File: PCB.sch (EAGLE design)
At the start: 38 parts, among them IC1 MAX13448E, IC2 MAX13487E, IC3 LP2981A-50_DBV_5, IC4 TXB0101, IC5 TXB0101, IC6 SN74LVC2G04_DBV_6, IC7 MAX232E, IC8 SN74LVC1G11_DBV_6

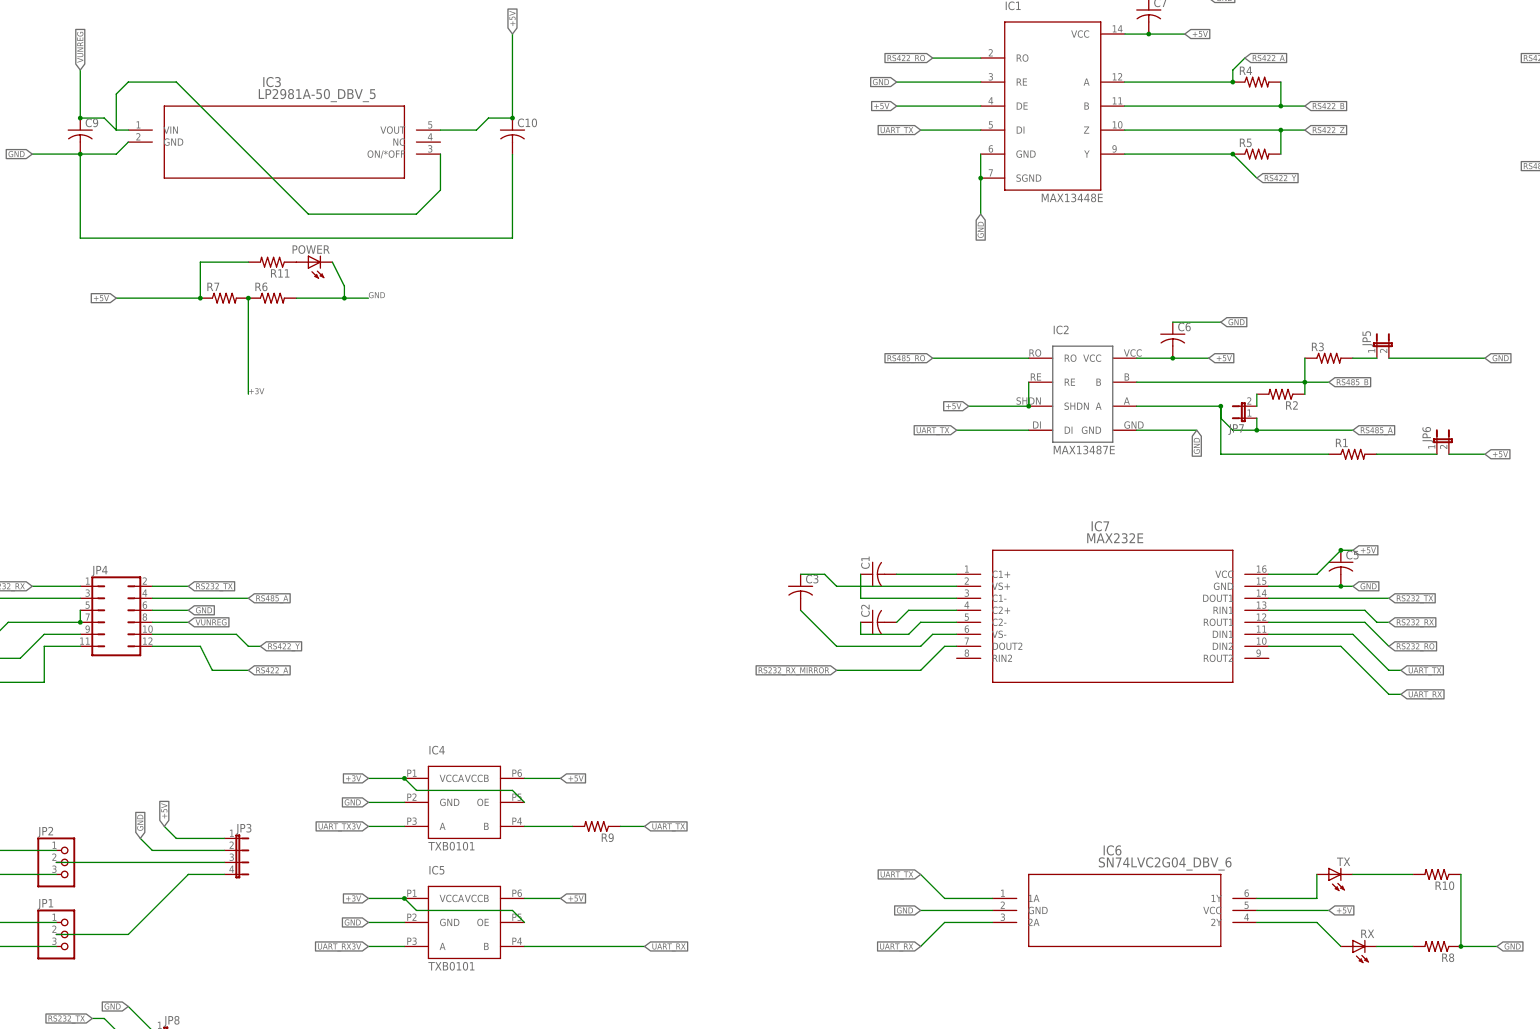
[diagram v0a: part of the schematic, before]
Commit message: Layout and silk screen tweaks
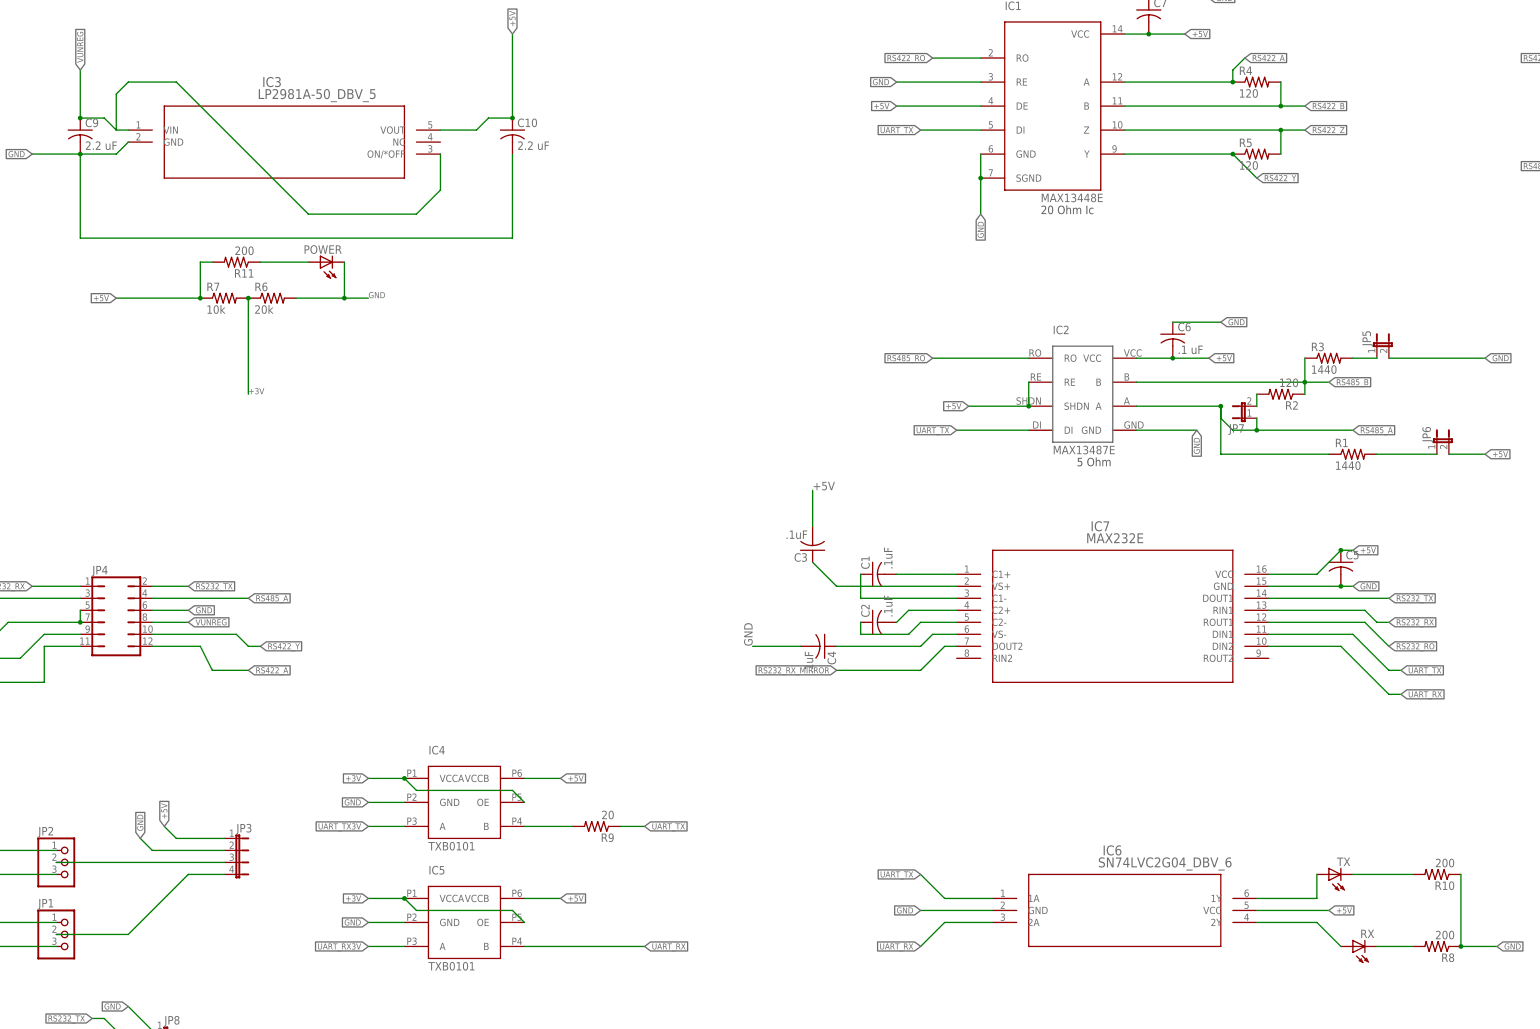
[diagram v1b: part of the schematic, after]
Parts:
- added C4: .1uF, adafruit:C-USC1206
- C1, C2, C3: value (none) -> .1uF
- C10, C9: value (none) -> 2.2 uF
- C6: value (none) -> .1 uF
- R1, R3: value (none) -> 1440
- R10, R11, R8: value (none) -> 200
- R2, R4, R5: value (none) -> 120
- R6: value (none) -> 20k
- R7: value (none) -> 10k
- R9: value (none) -> 20
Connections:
- net +5V: now also C3.2
- net GND: now also C4.2
- net RS232_VS-: now also C4.1; no longer C3.2
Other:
- note added: "20 Ohm Ic"
- note added: "5 Ohm"
- moved on the sheet: C3, POWER, R11
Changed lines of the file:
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@@
 <parts>
 <part name="IC2" library="maximIntegrated" deviceset="MAX13487E" device=""/>
-<part name="C6" library="adafruit" deviceset="C-US" device="C1206"/>
-<part name="R1" library="adafruit" deviceset="R-US_" device="M1206"/>
-<part name="R2" library="adafruit" deviceset="R-US_" device="M1206"/>
-<part name="R3" library="adafruit" deviceset="R-US_" device="M1206"/>
-<part name="C1" library="adafruit" deviceset="C-US" device="C1206"/>
-<part name="C2" library="adafruit" deviceset="C-US" device="C1206"/>
-<part name="C3" library="adafruit" deviceset="C-US" device="C1206"/>
+<part name="C6" library="adafruit" deviceset="C-US" device="C1206" value=".1 uF"/>
+<part name="R1" library="adafruit" deviceset="R-US_" device="M1206" value="1440"/>
+<part name="R2" library="adafruit" deviceset="R-US_" device="M1206" value="120"/>
+<part name="R3" library="adafruit" deviceset="R-US_" device="M1206" value="1440"/>
+<part name="C1" library="adafruit" deviceset="C-US" device="C1206" value=".1uF"/>
+<part name="C2" library="adafruit" deviceset="C-US" device="C1206" value=".1uF"/>
+<part name="C3" library="adafruit" deviceset="C-US" device="C1206" value=".1uF"/>
 <part name="C5" library="adafruit" deviceset="C-US" device="C1206"/>
 <part name="IC3" library="TI" deviceset="LP2981A-50_DBV_5" device=""/>
-<part name="C9" library="adafruit" deviceset="C-US" device="C1206"/>
-<part name="C10" library="adafruit" deviceset="C-US" device="C1206"/>
+<part name="C9" library="adafruit" deviceset="C-US" device="C1206" value="2.2 uF"/>
+<part name="C10" library="adafruit" deviceset="C-US" device="C1206" value="2.2 uF"/>
 <part name="JP3" library="jumper" deviceset="JP4E" device=""/>
-<part name="R6" library="adafruit" deviceset="R-US_" device="M1206"/>
-<part name="R7" library="adafruit" deviceset="R-US_" device="M1206"/>
+<part name="R6" library="adafruit" deviceset="R-US_" device="M1206" value="20k"/>
+<part name="R7" library="adafruit" deviceset="R-US_" device="M1206" value="10k"/>
 <part name="IC1" library="maximIntegrated" deviceset="MAX13448E" device=""/>
-<part name="R4" library="adafruit" deviceset="R-US_" device="R1206"/>
-<part name="R5" library="adafruit" deviceset="R-US_" device="R1206"/>
+<part name="R4" library="adafruit" deviceset="R-US_" device="R1206" value="120"/>
+<part name="R5" library="adafruit" deviceset="R-US_" device="R1206" value="120"/>
 <part name="C7" library="adafruit" deviceset="C-US" device="C1206"/>
 <part name="IC4" library="TI" deviceset="TXB0101" device=""/>
@@
 <part name="IC7" library="TI" deviceset="MAX232E_D_16" device="" value="MAX232E"/>
 <part name="JP4" library="jumper" deviceset="JP6Q" device=""/>
-<part name="R9" library="adafruit" deviceset="R-US_" device="M1206"/>
+<part name="R9" library="adafruit" deviceset="R-US_" device="M1206" value="20"/>
 <part name="JP1" library="adafruit" deviceset="PINHD-1X3" device=""/>
 <part name="IC8" library="TI" deviceset="SN74LVC1G11_DBV_6" device=""/>
@@
 <part name="TX" library="adafruit" deviceset="LED" device="CHIP-LED0603"/>
 <part name="RX" library="adafruit" deviceset="LED" device="CHIP-LED0603"/>
-<part name="R8" library="adafruit" deviceset="R-US_" device="M1206"/>
-<part name="R10" library="adafruit" deviceset="R-US_" device="M1206"/>
-<part name="R11" library="adafruit" deviceset="R-US_" device="M1206"/>
+<part name="R8" library="adafruit" deviceset="R-US_" device="M1206" value="200"/>
+<part name="R10" library="adafruit" deviceset="R-US_" device="M1206" value="200"/>
+<part name="R11" library="adafruit" deviceset="R-US_" device="M1206" value="200"/>
 <part name="POWER" library="adafruit" deviceset="LED" device="CHIP-LED0603"/>
 <part name="JP8" library="jumper" deviceset="JP2E" device=""/>
+<part name="C4" library="adafruit" deviceset="C-US" device="C1206" value=".1uF"/>
 </parts>
 <sheets>
@@
 <plain>
 <frame x1="-264.16" y1="12.7" x2="256.54" y2="302.26" columns="8" rows="5" layer="91"/>
+<text x="12.7" y="233.68" size="1.778" layer="97">20 Ohm Ic</text>
+<text x="20.32" y="180.34" size="1.778" layer="97">5 Ohm</text>
 </plain>
 <instances>
@@
 <instance part="C1" gate="G$1" x="-22.86" y="157.48" rot="R90"/>
 <instance part="C2" gate="G$1" x="-22.86" y="147.32" rot="R90"/>
-<instance part="C3" gate="G$1" x="-38.1" y="154.94"/>
+<instance part="C3" gate="G$1" x="-35.56" y="162.56" rot="R180"/>
 <instance part="C5" gate="G$1" x="76.2" y="160.02"/>
 <instance part="IC3" gate="A" x="-180.34" y="251.46"/>
@@
 <instance part="R8" gate="G$1" x="96.52" y="78.74" rot="R180"/>
 <instance part="R10" gate="G$1" x="96.52" y="93.98" rot="R180"/>
-<instance part="R11" gate="G$1" x="-149.86" y="223.52" rot="R180"/>
-<instance part="POWER" gate="G$1" x="-142.24" y="223.52" rot="R90"/>
+<instance part="R11" gate="G$1" x="-157.48" y="223.52" rot="R180"/>
+<instance part="POWER" gate="G$1" x="-139.7" y="223.52" rot="R90"/>
 <instance part="JP8" gate="1" x="-172.72" y="58.42" rot="R270"/>
+<instance part="C4" gate="G$1" x="-33.02" y="142.24" rot="R270"/>
 </instances>
 <busses>
@@
 <label x="-182.88" y="215.9" size="1.27" layer="95" rot="R180" xref="yes"/>
 <pinref part="R11" gate="G$1" pin="2"/>
-<wire x1="-154.94" y1="223.52" x2="-165.1" y2="223.52" width="0.1524" layer="91"/>
+<wire x1="-162.56" y1="223.52" x2="-165.1" y2="223.52" width="0.1524" layer="91"/>
 <wire x1="-165.1" y1="223.52" x2="-165.1" y2="215.9" width="0.1524" layer="91"/>
 <junction x="-165.1" y="215.9"/>
@@
 <wire x1="73.66" y1="86.36" x2="58.42" y2="86.36" width="0.1524" layer="91"/>
 <label x="73.66" y="86.36" size="1.27" layer="95" xref="yes"/>
+</segment>
+<segment>
+<pinref part="C3" gate="G$1" pin="2"/>
+<wire x1="-35.56" y1="167.64" x2="-35.56" y2="175.26" width="0.1524" layer="91"/>
+<label x="-35.56" y="175.26" size="1.778" layer="95"/>
 </segment>
 </net>
@@
 <pinref part="POWER" gate="G$1" pin="C"/>
 <wire x1="-134.62" y1="215.9" x2="-129.54" y2="215.9" width="0.1524" layer="91"/>
-<wire x1="-137.16" y1="223.52" x2="-134.62" y2="218.44" width="0.1524" layer="91"/>
-<wire x1="-134.62" y1="218.44" x2="-134.62" y2="215.9" width="0.1524" layer="91"/>
+<wire x1="-134.62" y1="223.52" x2="-134.62" y2="215.9" width="0.1524" layer="91"/>
 <junction x="-134.62" y="215.9"/>
 </segment>
@@
 <wire x1="-175.26" y1="60.96" x2="-180.34" y2="66.04" width="0.1524" layer="91"/>
 <label x="-180.34" y="66.04" size="1.27" layer="95" rot="R180" xref="yes"/>
+</segment>
+<segment>
+<pinref part="C4" gate="G$1" pin="2"/>
+<wire x1="-38.1" y1="142.24" x2="-48.26" y2="142.24" width="0.1524" layer="91"/>
+<label x="-48.26" y="142.24" size="1.778" layer="95" rot="R90"/>
 </segment>
 </net>
@@
 <wire x1="-5.08" y1="144.78" x2="-10.16" y2="144.78" width="0.1524" layer="91"/>
 <wire x1="-10.16" y1="144.78" x2="-12.7" y2="142.24" width="0.1524" layer="91"/>
-<pinref part="C3" gate="G$1" pin="2"/>
 <wire x1="-12.7" y1="142.24" x2="-30.48" y2="142.24" width="0.1524" layer="91"/>
-<wire x1="-30.48" y1="142.24" x2="-38.1" y2="149.86" width="0.1524" layer="91"/>
+<pinref part="C4" gate="G$1" pin="1"/>
 </segment>
 </net>
@@
 <segment>
 <pinref part="C3" gate="G$1" pin="1"/>
-<wire x1="-38.1" y1="157.48" x2="-33.02" y2="157.48" width="0.1524" layer="91"/>
-<wire x1="-33.02" y1="157.48" x2="-30.48" y2="154.94" width="0.1524" layer="91"/>
+<wire x1="-35.56" y1="160.02" x2="-30.48" y2="154.94" width="0.1524" layer="91"/>
 <pinref part="IC7" gate="A" pin="VS+"/>
 <wire x1="-30.48" y1="154.94" x2="-5.08" y2="154.94" width="0.1524" layer="91"/>
@@
 <pinref part="R11" gate="G$1" pin="1"/>
 <pinref part="POWER" gate="G$1" pin="A"/>
-</segment>
-</net>
+<wire x1="-152.4" y1="223.52" x2="-142.24" y2="223.52" width="0.1524" layer="91"/>
+</segment>
+</net>

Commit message: REV 1.2
Added onboard USB and supply isolation
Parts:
- removed C10: 2.2 uF, adafruit:C-USC1206
- removed IC4, IC5: TXB0101, TI:TXB0101
- removed JP2: (no value), adafruit:PINHD-1X3
- removed JP8: (no value), jumper:JP2E
- removed R11: 200, adafruit:R-US_M1206
- removed R7: 10k, adafruit:R-US_M1206
- added C11, C12, C13, C16, C17, C18, C8: .1uF, adafruit:C-USC1206
- added C14: .01 uF, adafruit:C-USC1206
- added C15: 2.2 uF, adafruit:C-USC1206
- added D1, D6: (no value), dp_devices:DIODE-SOT23
- added IC9: IC_FT230X-SSOP-16, dp_devices:IC_FT230X-SSOP-16
- added L1: (no value), dp_devices:FERRITE-1206
- added R12, R13: 27R, adafruit:R-US_R1206
- added U$1, U$2: TS5A3159-Q1, TI:TS5A3159-Q1
- added U1: DCH010505S_EDJ_4, TI:DCH010505S_EDJ_4
- added U3: REG101-3_DBV_5, TI:REG101-3_DBV_5
- added U5: ISO7231C_DW_16, TI:ISO7231C_DW_16
- added X1: USB-A, adafruit:USB-A
- C5: value (none) -> .1uF
- C7: value (none) -> .1 uF
- JP1: device adafruit:PINHD-1X3 -> jumper:JP1E
- POWER, RX, TX: device adafruit:LEDCHIP-LED0603 -> adafruit:LEDSMT1206
- R6: value 20k -> 200
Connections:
- removed net N$2: POWER.A, R11.1
- removed net RS232_RX_MIRROR: IC7.DOUT2, JP8.3
- removed net RX: JP1.2, JP3.4
- removed net TX: JP2.2, JP3.3
- removed net UART_RX3V: IC5.A, JP1.3
- removed net UART_TX3V: IC4.A, JP2.3
- removed net UART_TXLOAD: IC4.B, JP2.1, R9.2
- removed net VUNREG: C9.1, IC3.ON/*OFF, IC3.VIN, JP4.8
- new net BT_RX: JP3.4, U$1.NC
- new net BT_TX: JP3.3, U$2.NC
- new net EXT_5V: C18.1, D6.A, IC3.VOUT
- new net EXT_GND: C16.2, C18.2, C9.2, IC3.GND, JP1.2, JP4.5, U1.VI-
- new net EXT_VCC: C9.1, IC3.ON/*OFF, IC3.VIN, JP1.1, JP4.7
- new net N$10: C11.2, R13.1, X1.D-
- new net N$11: C14.1, U3.NR/ADJUST
- new net N$4: IC9.TXD, U5.INB
- new net N$5: IC9.RXD, U5.OUTC
- new net N$6: POWER.C, R6.2
- new net N$7: IC9.USB-, R13.2
- new net N$8: IC9.USB+, R12.2
- new net N$9: C8.2, R12.1, X1.D+
- new net UART_TX_1: R9.2, U$2.COM
- new net USB_3V: C13.1, IC9.!RESET, IC9.3V3OUT, IC9.VCCIO, U5.INA, U5.NC_2, U5.VCC1
- new net USB_5V: D1.A, IC9.VCC, L1.2
- new net USB_GND: C11.1, C12.1, C13.2, C8.1, IC9.GND@1, IC9.GND@2, U5.GND1, U5.GND1_2, X1.GND
- new net USB_RX: U$1.NO, U5.INC
- new net USB_SWITCH: U$1.IN, U$2.IN, U5.OUTA
- new net USB_TX: U$2.NO, U5.OUTB
- new net USB_VCC: C16.1, D1.C, D6.C, U1.VI+
- new net VCC_USB: C12.2, L1.1, X1.VBUS
- net +3V: now also C15.1, U$1.VCC, U$2.VCC, U3.VOUT, U5.EN2, U5.VCC2; no longer IC4.OE, IC4.VCCA, IC5.OE, IC5.VCCA, R6.1, R7.2
- net +5V: now also C17.1, POWER.A, U1.VO+, U3.ENABLE, U3.VIN; no longer C10.1, IC3.VOUT, IC4.VCCB, IC5.VCCB, R11.2, R7.1
- net GND: now also C14.2, C15.2, C17.2, JP4.8, R6.1, U$1.GND, U$2.GND, U1.VO-, U3.GND, U5.GND2, U5.GND2_2; no longer C10.2, C9.2, IC3.GND, IC4.GND, IC5.GND, JP4.5, JP4.7, JP8.1, POWER.C, R6.2
- net RS232_RO: now also IC8.B; no longer IC8.C
- net RS232_RX: now also JP4.3; no longer JP4.1
- net RS232_TX: now also JP4.4; no longer JP4.2, JP8.2
- net RS485_A: now also JP4.2; no longer JP4.4
- net RS485_B: now also JP4.1; no longer JP4.3
- net RS485_RO: now also IC8.C; no longer IC8.B
- net UART_RX: now also U$1.COM; no longer IC5.B, IC7.DIN2, JP1.1
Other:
- note added: "Logic Buffer to drive RX and TX LED's Buffer reduces load on line and isolates LED's from data bus"
- note added: "Power supply: + 5V: Supplied through either USB power or external 5V to 16V source. External power source isolated through DC-DC converter. +3V: Stepped down from 5V rail via LDO."
- note added: "USB UART lines electrically isolated. UART connection from FTDI chip and external BT module switched through analog switch. Switch is normally set for BT mode. Applying power via USB switches the IC to USB mode."
- moved on the sheet: C1, C2, C3, C4, C5, C6, C7, C9, IC1, IC2, IC3, IC6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

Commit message: updates to document V1rA Eratta
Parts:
- C11, C8: value .1uF -> 47pF
- C12: value .1uF -> .01uF
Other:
- note added: "Jumper Wire"
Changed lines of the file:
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@@
 <part name="R12" library="adafruit" deviceset="R-US_" device="R1206" value="27R"/>
 <part name="R13" library="adafruit" deviceset="R-US_" device="R1206" value="27R"/>
-<part name="C8" library="adafruit" deviceset="C-US" device="C1206" value=".1uF"/>
-<part name="C11" library="adafruit" deviceset="C-US" device="C1206" value=".1uF"/>
-<part name="C12" library="adafruit" deviceset="C-US" device="C1206" value=".1uF"/>
+<part name="C8" library="adafruit" deviceset="C-US" device="C1206" value="47pF"/>
+<part name="C11" library="adafruit" deviceset="C-US" device="C1206" value="47pF"/>
+<part name="C12" library="adafruit" deviceset="C-US" device="C1206" value=".01uF"/>
 <part name="C13" library="adafruit" deviceset="C-US" device="C1206" value=".1uF"/>
 <part name="U1" library="TI" deviceset="DCH010505S_EDJ_4" device=""/>
@@
 <text x="-226.06" y="66.04" size="1.778" layer="91">Logic Buffer to drive RX and TX LED's
 Buffer reduces load on line and isolates LED's from data bus</text>
+<text x="-218.44" y="190.5" size="1.778" layer="97">Jumper Wire</text>
+<wire x1="-226.06" y1="195.58" x2="-142.24" y2="195.58" width="0.1524" layer="97"/>
+<wire x1="-142.24" y1="195.58" x2="-142.24" y2="175.26" width="0.1524" layer="97"/>
+<wire x1="-142.24" y1="175.26" x2="-226.06" y2="175.26" width="0.1524" layer="97"/>
+<wire x1="-226.06" y1="175.26" x2="-226.06" y2="195.58" width="0.1524" layer="97"/>
+<rectangle x1="-202.946" y1="181.864" x2="-170.18" y2="183.896" layer="97"/>
 </plain>
 <instances>
@@
 <label x="-99.06" y="203.2" size="1.778" layer="95"/>
 </segment>
+<segment>
+<wire x1="-203.2" y1="182.88" x2="-205.74" y2="182.88" width="0.1524" layer="91"/>
+<label x="-205.74" y="182.88" size="1.778" layer="95" rot="R180" xref="yes"/>
+</segment>
 </net>
 <net name="USB_VCC" class="0">
@@
 <label x="129.54" y="53.34" size="1.778" layer="95" rot="R180"/>
 </segment>
-</net>
+<segment>
+<wire x1="-170.18" y1="182.88" x2="-165.1" y2="182.88" width="0.1524" layer="91"/>
+<label x="-165.1" y="182.88" size="1.778" layer="95" xref="yes"/>
+</segment>
+</net>
